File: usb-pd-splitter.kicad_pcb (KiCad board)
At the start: 2 copper layers, 0 parts

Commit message: layout done, routing half way
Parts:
- added J1: USB_C_Receptacle_USB2.0_14P, cl_Connector_USB:USB_C_Receptacle_GCT_USB4110, F.Cu at (118.5, 101.0)
- added J2: USB_C_Receptacle_USB2.0_14P, cl_Connector_USB:USB_C_Receptacle_GCT_USB4110, F.Cu at (118.5, 122.0)
- added J3: USB_C_Receptacle_USB2.0_14P, cl_Connector_USB:USB_C_Receptacle_GCT_USB4110, F.Cu at (146.5, 112.0)
- added R1: 5.1k, Resistor_SMD:R_0805_2012Metric_Pad1.20x1.40mm_HandSolder, F.Cu at (126.0, 118.0)
- added R2: 5.1k, Resistor_SMD:R_0805_2012Metric_Pad1.20x1.40mm_HandSolder, F.Cu at (126.0, 125.5)
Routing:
- net /CC1_POWER: track 0.00 -> 34.1 mm, vias 0 -> 2
- net /D-: track 0.00 -> 30.1 mm
- net /D+: track 0.00 -> 29.4 mm, vias 0 -> 2
- net /CC2_POWER: track 0.00 -> 23.7 mm
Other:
- board outline added: 35 x 35 mm
- board text added: "DAT IN"
- board text added: "OUT"
- board text added: "POW IN"

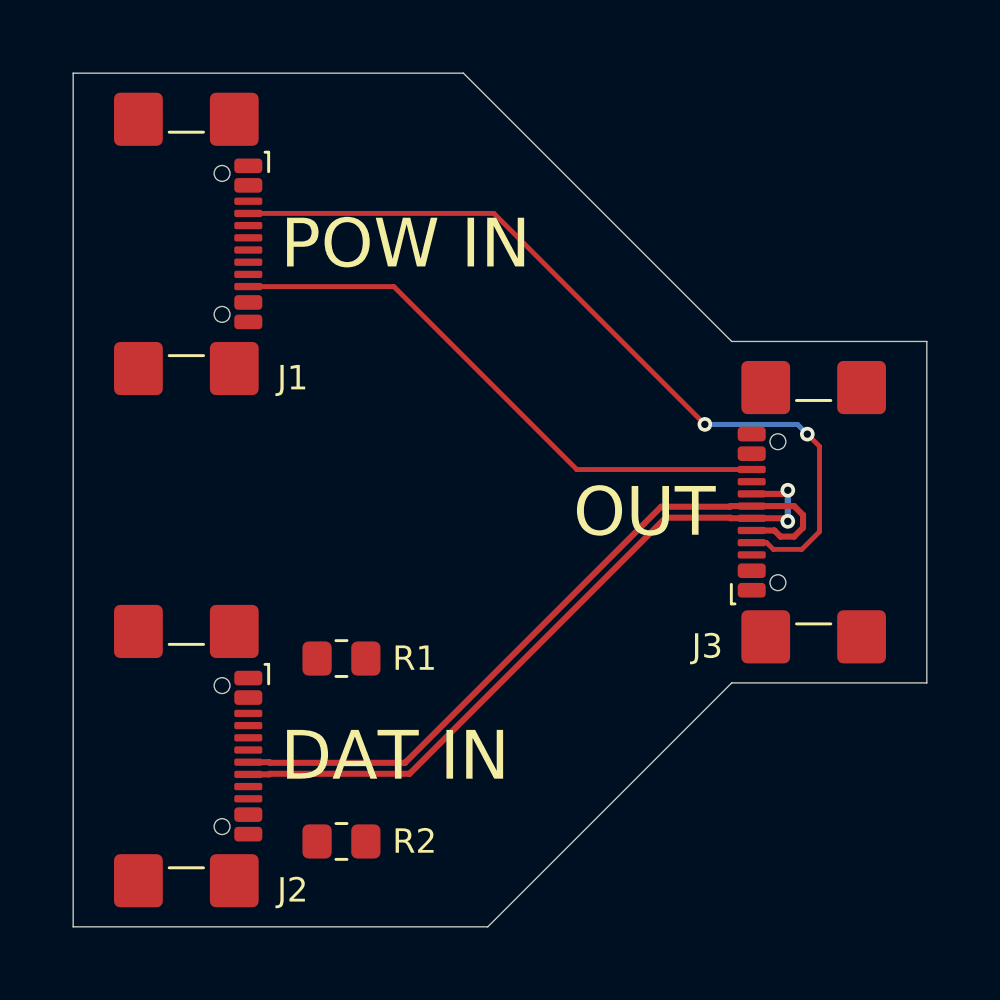
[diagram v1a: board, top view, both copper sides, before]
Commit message: routing complete, drc pass
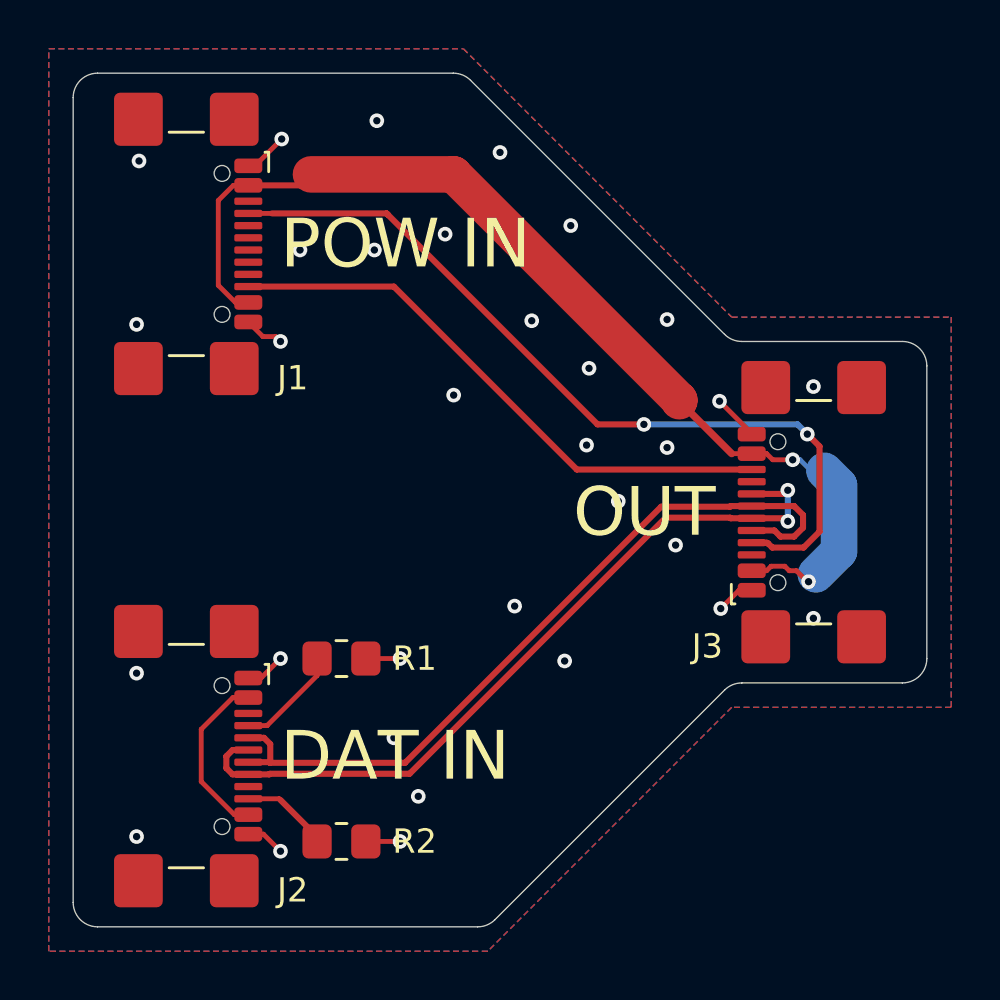
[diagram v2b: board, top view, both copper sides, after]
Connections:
- J1 pad A8: (no net) -> unconnected-(J1-SBU1-PadA8)
- J1 pad B8: (no net) -> unconnected-(J1-SBU2-PadB8)
- J2 pad A4: unconnected-(J2-VBUS-PadA4) -> /VBUS_NC
- J2 pad A8: (no net) -> unconnected-(J2-SBU1-PadA8)
- J2 pad A9: unconnected-(J2-VBUS-PadA4)_1 -> /VBUS_NC
- J2 pad B4: unconnected-(J2-VBUS-PadA4)_3 -> /VBUS_NC
- J2 pad B8: (no net) -> unconnected-(J2-SBU2-PadB8)
- J2 pad B9: unconnected-(J2-VBUS-PadA4)_2 -> /VBUS_NC
- J3 pad A8: (no net) -> unconnected-(J3-SBU1-PadA8)
- J3 pad B8: (no net) -> unconnected-(J3-SBU2-PadB8)
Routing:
- net VBUS: track 0.00 -> 42.9 mm, vias 0 -> 2
- net GND: track 0.00 -> 13.0 mm, vias 0 -> 32
- net /VBUS_NC: track 0.00 -> 7.10 mm
- net Net-(J2-CC1): track 0.00 -> 4.37 mm
- net Net-(J2-CC2): track 0.00 -> 3.66 mm
- net /D+: track 29.4 -> 31.9 mm
- net /D-: track 30.1 -> 31.9 mm
- added copper zone on B.Cu, net GND
- added copper zone on F.Cu, net GND
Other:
- outline, holes or cut-outs redrawn

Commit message: release: prepare hardware v1.1.0
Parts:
- added D1: Green, LED_SMD:LED_0805_2012Metric, F.Cu at (132.6, 105.4)
- added R3: 10k, Resistor_SMD:R_0805_2012Metric_Pad1.20x1.40mm_HandSolder, F.Cu at (134.6, 105.4)
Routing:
- net VBUS: track 42.9 -> 46.6 mm
- net Net-(D1-K): track 0.00 -> 2.80 mm
